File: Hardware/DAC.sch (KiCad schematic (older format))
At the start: 10 parts, among them U11 PCM1796

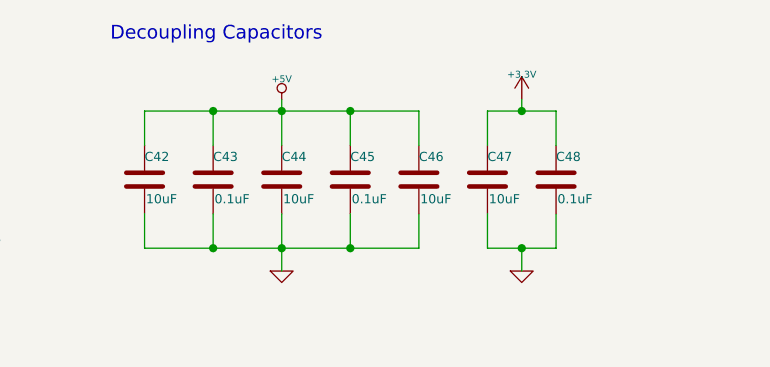
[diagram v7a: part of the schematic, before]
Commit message: Fixed schematic errors, added muse-v2-lib
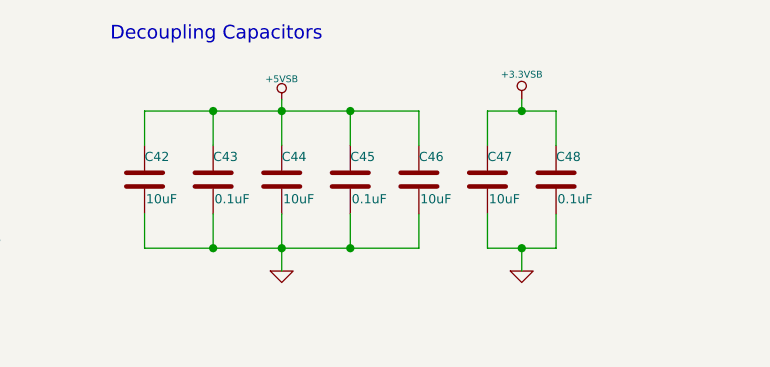
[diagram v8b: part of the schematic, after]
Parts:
- C42, C44, C46, C47: footprint (none) -> Capacitors_SMD:c_elec_4x4.5
- C43, C45, C48: footprint (none) -> Capacitors_SMD:C_0402
- C49: footprint (none) -> Capacitors_SMD:c_elec_6.3x7.7
- R25: footprint (none) -> Resistors_SMD:R_0402
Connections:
- net +3V3 is gone; now on net +3.3VSB: C47.1, C48.1
- net +5V is gone; now on net +5VSB: C42.1, C43.1, C44.1, C45.1, C46.1
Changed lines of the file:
@@
 Pulled HIGH for\nI2C mode
 $Comp
-L GND-RESCUE-museV2-RESCUE-museV2 #PWR067
+L GND-RESCUE-museV2-RESCUE-museV2 #PWR74
 U 1 1 57F8A4EE
 P 8150 3350
-F 0 "#PWR067" H 8150 3350 30  0001 C CNN
+F 0 "#PWR74" H 8150 3350 30  0001 C CNN
 F 1 "GND" H 8150 3280 30  0001 C CNN
 F 2 "" H 8150 3350 60  0000 C CNN
@@
 F 0 "C48" H 8300 3050 40  0000 L CNN
 F 1 "0.1uF" H 8306 2865 40  0000 L CNN
-F 2 "" H 8338 2800 30  0000 C CNN
+F 2 "Capacitors_SMD:C_0402" H 8338 2800 30  0001 C CNN
 F 3 "" H 8300 2950 60  0000 C CNN
 	1    8300 2950
@@
 F 0 "C47" H 8000 3050 40  0000 L CNN
 F 1 "10uF" H 8006 2865 40  0000 L CNN
-F 2 "" H 8038 2800 30  0000 C CNN
+F 2 "Capacitors_SMD:c_elec_4x4.5" H 8038 2800 30  0001 C CNN
 F 3 "" H 8000 2950 60  0000 C CNN
 	1    8000 2950
 	1    0    0    -1
 $EndComp
-$Comp
-L +3.3V-RESCUE-museV2 #PWR068
-U 1 1 57F8A502
-P 8150 2600
-F 0 "#PWR068" H 8150 2560 30  0001 C CNN
-F 1 "+3.3V" H 8150 2710 30  0000 C CNN
-F 2 "" H 8150 2600 60  0000 C CNN
-F 3 "" H 8150 2600 60  0000 C CNN
-	1    8150 2600
-	1    0    0    -1
-$EndComp
-$Comp
-L +5V #PWR069
-U 1 1 57F8A508
-P 7100 2600
-F 0 "#PWR069" H 7100 2690 20  0001 C CNN
-F 1 "+5V" H 7100 2690 30  0000 C CNN
-F 2 "" H 7100 2600 60  0000 C CNN
-F 3 "" H 7100 2600 60  0000 C CNN
-	1    7100 2600
-	1    0    0    -1
-$EndComp
 Text Notes 6350 2350 0    60   ~ 0
 Decoupling Capacitors
 $Comp
-L GND-RESCUE-museV2-RESCUE-museV2 #PWR070
+L GND-RESCUE-museV2-RESCUE-museV2 #PWR73
 U 1 1 57F8A50F
 P 7100 3350
-F 0 "#PWR070" H 7100 3350 30  0001 C CNN
+F 0 "#PWR73" H 7100 3350 30  0001 C CNN
 F 1 "GND" H 7100 3280 30  0001 C CNN
 F 2 "" H 7100 3350 60  0000 C CNN
@@
 F 0 "C46" H 7700 3050 40  0000 L CNN
 F 1 "10uF" H 7706 2865 40  0000 L CNN
-F 2 "" H 7738 2800 30  0000 C CNN
+F 2 "Capacitors_SMD:c_elec_4x4.5" H 7738 2800 30  0001 C CNN
 F 3 "" H 7700 2950 60  0000 C CNN
 	1    7700 2950
@@
 F 0 "C45" H 7400 3050 40  0000 L CNN
 F 1 "0.1uF" H 7406 2865 40  0000 L CNN
-F 2 "" H 7438 2800 30  0000 C CNN
+F 2 "Capacitors_SMD:C_0402" H 7438 2800 30  0001 C CNN
 F 3 "" H 7400 2950 60  0000 C CNN
 	1    7400 2950
@@
 F 0 "C44" H 7100 3050 40  0000 L CNN
 F 1 "10uF" H 7106 2865 40  0000 L CNN
-F 2 "" H 7138 2800 30  0000 C CNN
+F 2 "Capacitors_SMD:c_elec_4x4.5" H 7138 2800 30  0001 C CNN
 F 3 "" H 7100 2950 60  0000 C CNN
 	1    7100 2950
@@
 F 0 "C43" H 6800 3050 40  0000 L CNN
 F 1 "0.1uF" H 6806 2865 40  0000 L CNN
-F 2 "" H 6838 2800 30  0000 C CNN
+F 2 "Capacitors_SMD:C_0402" H 6838 2800 30  0001 C CNN
 F 3 "" H 6800 2950 60  0000 C CNN
 	1    6800 2950
@@
 F 0 "C42" H 6500 3050 40  0000 L CNN
 F 1 "10uF" H 6506 2865 40  0000 L CNN
-F 2 "" H 6538 2800 30  0000 C CNN
+F 2 "Capacitors_SMD:c_elec_4x4.5" H 6538 2800 30  0001 C CNN
 F 3 "" H 6500 2950 60  0000 C CNN
 	1    6500 2950
@@
 F 0 "U11" H 4700 3450 60  0000 C CNN
 F 1 "PCM1796" H 5300 1500 60  0000 C CNN
-F 2 "" H 4600 3400 60  0000 C CNN
+F 2 "" H 4600 3400 60  0001 C CNN
 F 3 "" H 4600 3400 60  0000 C CNN
 	1    4600 3400
@@
 $EndComp
 $Comp
-L GND-RESCUE-museV2-RESCUE-museV2 #PWR071
+L GND-RESCUE-museV2-RESCUE-museV2 #PWR77
 U 1 1 57F8A564
 P 6100 5450
-F 0 "#PWR071" H 6100 5450 30  0001 C CNN
+F 0 "#PWR77" H 6100 5450 30  0001 C CNN
 F 1 "GND" H 6100 5380 30  0001 C CNN
 F 2 "" H 6100 5450 60  0000 C CNN
@@
 F 0 "R25" V 6180 5150 40  0000 C CNN
 F 1 "10K" V 6107 5151 40  0000 C CNN
-F 2 "" V 6030 5150 30  0000 C CNN
+F 2 "Resistors_SMD:R_0402" V 6030 5150 30  0001 C CNN
 F 3 "" H 6100 5150 30  0000 C CNN
 	1    6100 5150
@@
 $EndComp
 $Comp
-L GND-RESCUE-museV2-RESCUE-museV2 #PWR072
+L GND-RESCUE-museV2-RESCUE-museV2 #PWR76
 U 1 1 57F8A571
 P 5800 5450
-F 0 "#PWR072" H 5800 5450 30  0001 C CNN
+F 0 "#PWR76" H 5800 5450 30  0001 C CNN
 F 1 "GND" H 5800 5380 30  0001 C CNN
 F 2 "" H 5800 5450 60  0000 C CNN
@@
 F 0 "C49" H 2800 3950 40  0000 L CNN
 F 1 "47uF" H 2806 3765 40  0000 L CNN
-F 2 "" H 2838 3700 30  0000 C CNN
+F 2 "Capacitors_SMD:c_elec_6.3x7.7" H 2838 3700 30  0001 C CNN
 F 3 "" H 2800 3850 60  0000 C CNN
 	1    2800 3850
@@
 PCM1796 DAC
 $Comp
-L +3.3VSB #PWR073
+L +3.3VSB #PWR71
 U 1 1 57F8A57F
 P 4300 3300
-F 0 "#PWR073" H 4300 3260 30  0001 C CNN
+F 0 "#PWR71" H 4300 3260 30  0001 C CNN
 F 1 "+3.3VSB" H 4300 3410 30  0000 C CNN
 F 2 "" H 4300 3300 60  0000 C CNN
@@
 $EndComp
 $Comp
-L +5VSB #PWR074
+L +5VSB #PWR70
 U 1 1 57F8A585
 P 2800 3300
-F 0 "#PWR074" H 2800 3390 20  0001 C CNN
+F 0 "#PWR70" H 2800 3390 20  0001 C CNN
 F 1 "+5VSB" H 2800 3390 30  0000 C CNN
 F 2 "" H 2800 3300 60  0000 C CNN
@@
 $EndComp
 $Comp
-L +5VSB #PWR075
+L +5VSB #PWR72
 U 1 1 57F8A58B
 P 5800 3300
-F 0 "#PWR075" H 5800 3390 20  0001 C CNN
+F 0 "#PWR72" H 5800 3390 20  0001 C CNN
 F 1 "+5VSB" H 5800 3390 30  0000 C CNN
 F 2 "" H 5800 3300 60  0000 C CNN
@@
 NoConn ~ 5700 3850
 $Comp
-L +3.3VSB #PWR076
+L +3.3VSB #PWR75
 U 1 1 57F8A593
 P 2800 4500
-F 0 "#PWR076" H 2800 4460 30  0001 C CNN
+F 0 "#PWR75" H 2800 4460 30  0001 C CNN
 F 1 "+3.3VSB" H 2800 4610 30  0000 C CNN
 F 2 "" H 2800 4500 60  0000 C CNN
@@
 Text GLabel 8250 4700 2    60   Input ~ 0
 ANALOG_OUT_R
+$Comp
+L +3.3VSB #PWR69
+U 1 1 5859BC27
+P 8150 2600
+F 0 "#PWR69" H 8150 2560 30  0001 C CNN
+F 1 "+3.3VSB" H 8150 2710 30  0000 C CNN
+F 2 "" H 8150 2600 60  0000 C CNN
+F 3 "" H 8150 2600 60  0000 C CNN
+	1    8150 2600
+	1    0    0    -1
+$EndComp
+$Comp
+L +5VSB #PWR68
+U 1 1 5859DA88
+P 7100 2600
+F 0 "#PWR68" H 7100 2690 20  0001 C CNN
+F 1 "+5VSB" H 7100 2690 30  0000 C CNN
+F 2 "" H 7100 2600 60  0000 C CNN
+F 3 "" H 7100 2600 60  0000 C CNN
+	1    7100 2600
+	1    0    0    -1
+$EndComp
 $EndSCHEMATC
